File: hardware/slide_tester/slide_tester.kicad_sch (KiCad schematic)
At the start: 17 parts, among them J1 USB_A_Stacked, J2 Conn_01x01_Male, J3 Conn_01x01_Male, Q1 C32725, Q2 C32725, Q3 C32725

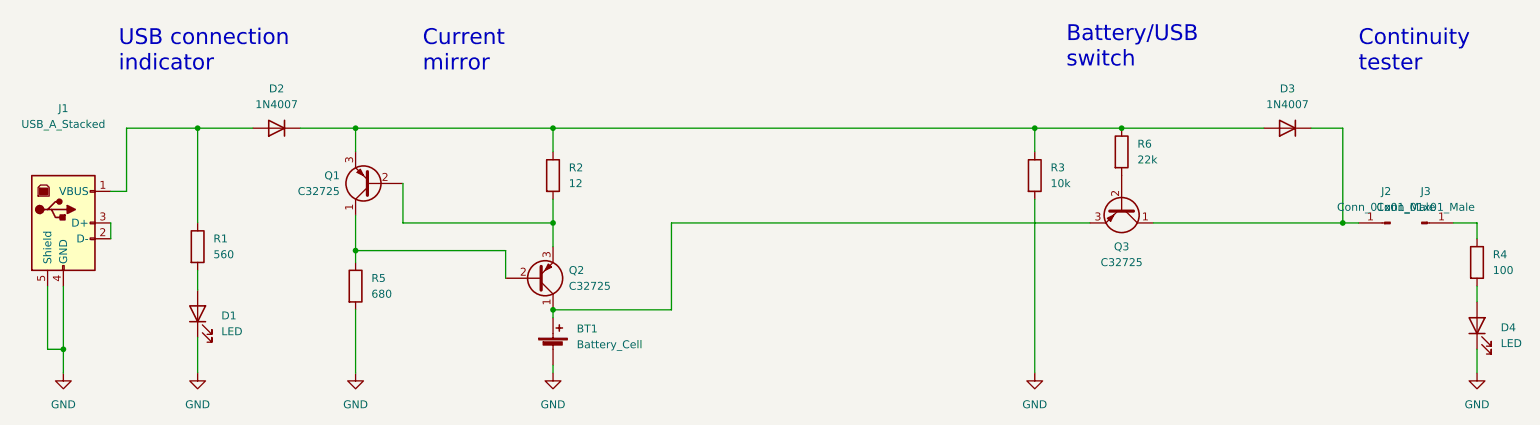
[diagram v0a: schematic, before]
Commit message: Add description, figures
Add gitignore and delete back-ups
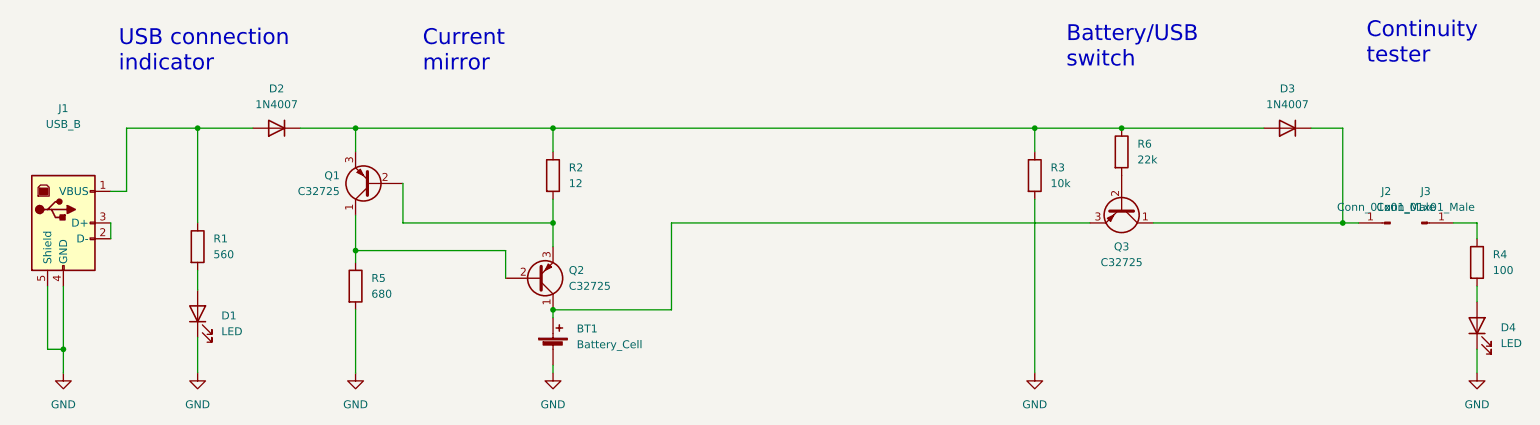
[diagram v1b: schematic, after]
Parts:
- J1: value USB_A_Stacked -> USB_B
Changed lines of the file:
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@@
     (effects (font (size 2.54 2.54)) (justify left bottom))
   )
-  (text "Continuity\ntester" (at 243.84 57.15 0)
+  (text "Continuity\ntester" (at 245.11 55.88 0)
     (effects (font (size 2.54 2.54)) (justify left bottom))
   )
@@
     (in_bom yes) (on_board yes) (fields_autoplaced)
     (property "Reference" "J1" (id 0) (at 35.56 62.865 0))
-    (property "Value" "USB_A_Stacked" (id 1) (at 35.56 65.405 0))
+    (property "Value" "USB_B" (id 1) (at 35.56 65.405 0))
     (property "Footprint" "Connector_USB:USB_B_OST_USB-B1HSxx_Horizontal" (id 2) (at 39.37 82.55 0)
       (effects (font (size 1.27 1.27)) hide)
@@
     )
     (path "/bedc87fe-7b02-49dd-b1d2-036c65f89b7f"
-      (reference "J1") (unit 1) (value "USB_A_Stacked") (footprint "Connector_USB:USB_B_OST_USB-B1HSxx_Horizontal")
+      (reference "J1") (unit 1) (value "USB_B") (footprint "Connector_USB:USB_B_OST_USB-B1HSxx_Horizontal")
     )
     (path "/cc2c1985-993f-48d0-bedd-833f9dbf4f5d"
